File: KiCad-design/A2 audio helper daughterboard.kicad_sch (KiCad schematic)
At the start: 3 parts, among them J15 PIN HEADER 2x6, J16 SJ1-3515N

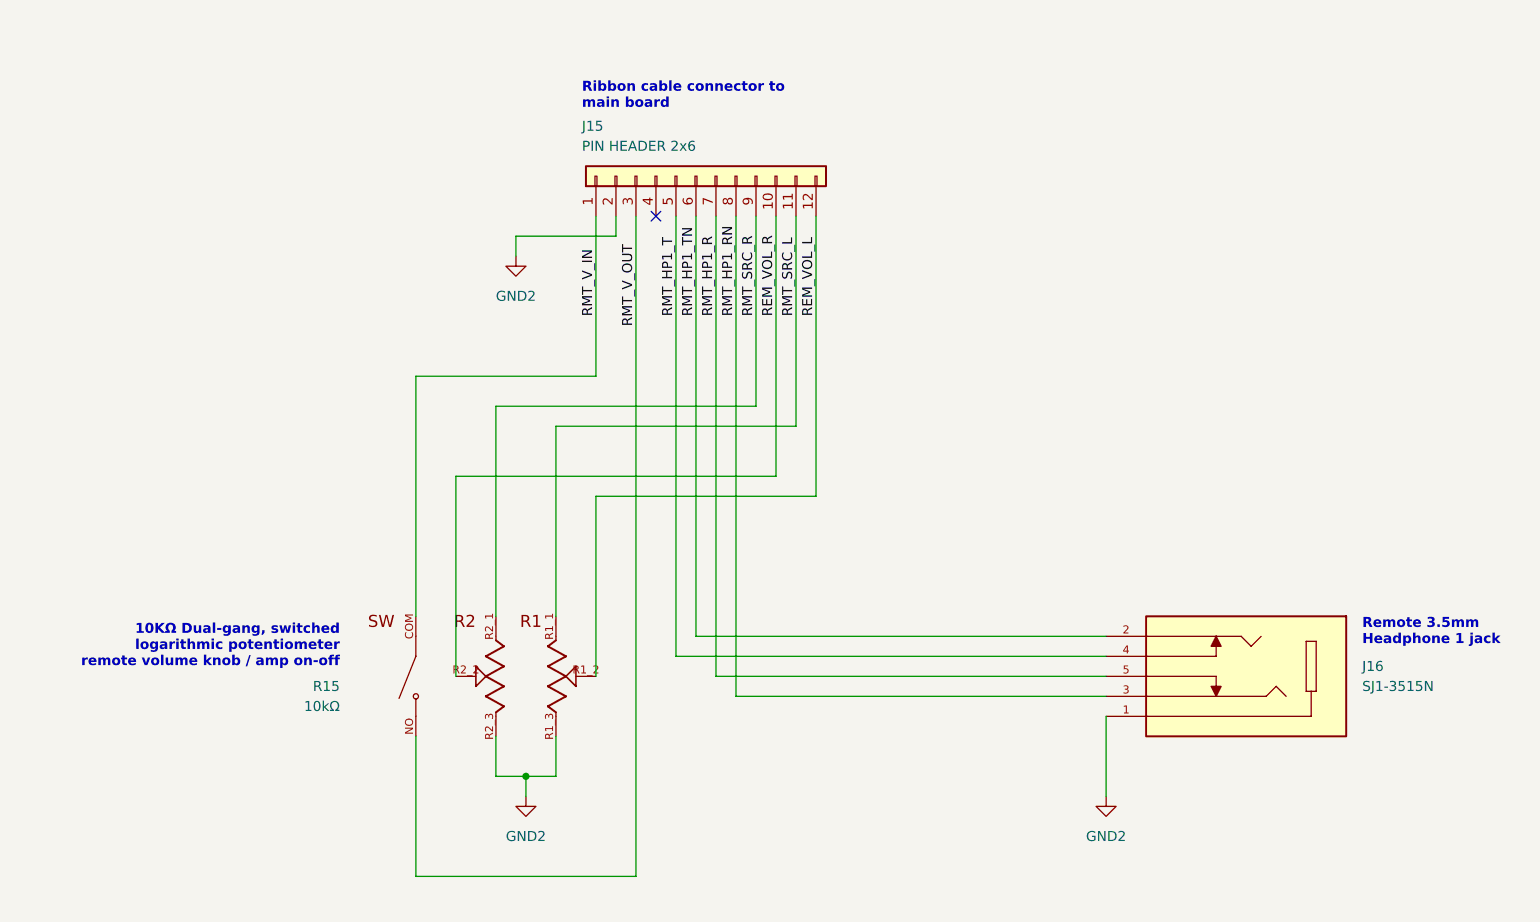
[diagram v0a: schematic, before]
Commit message: fixed dual headphones
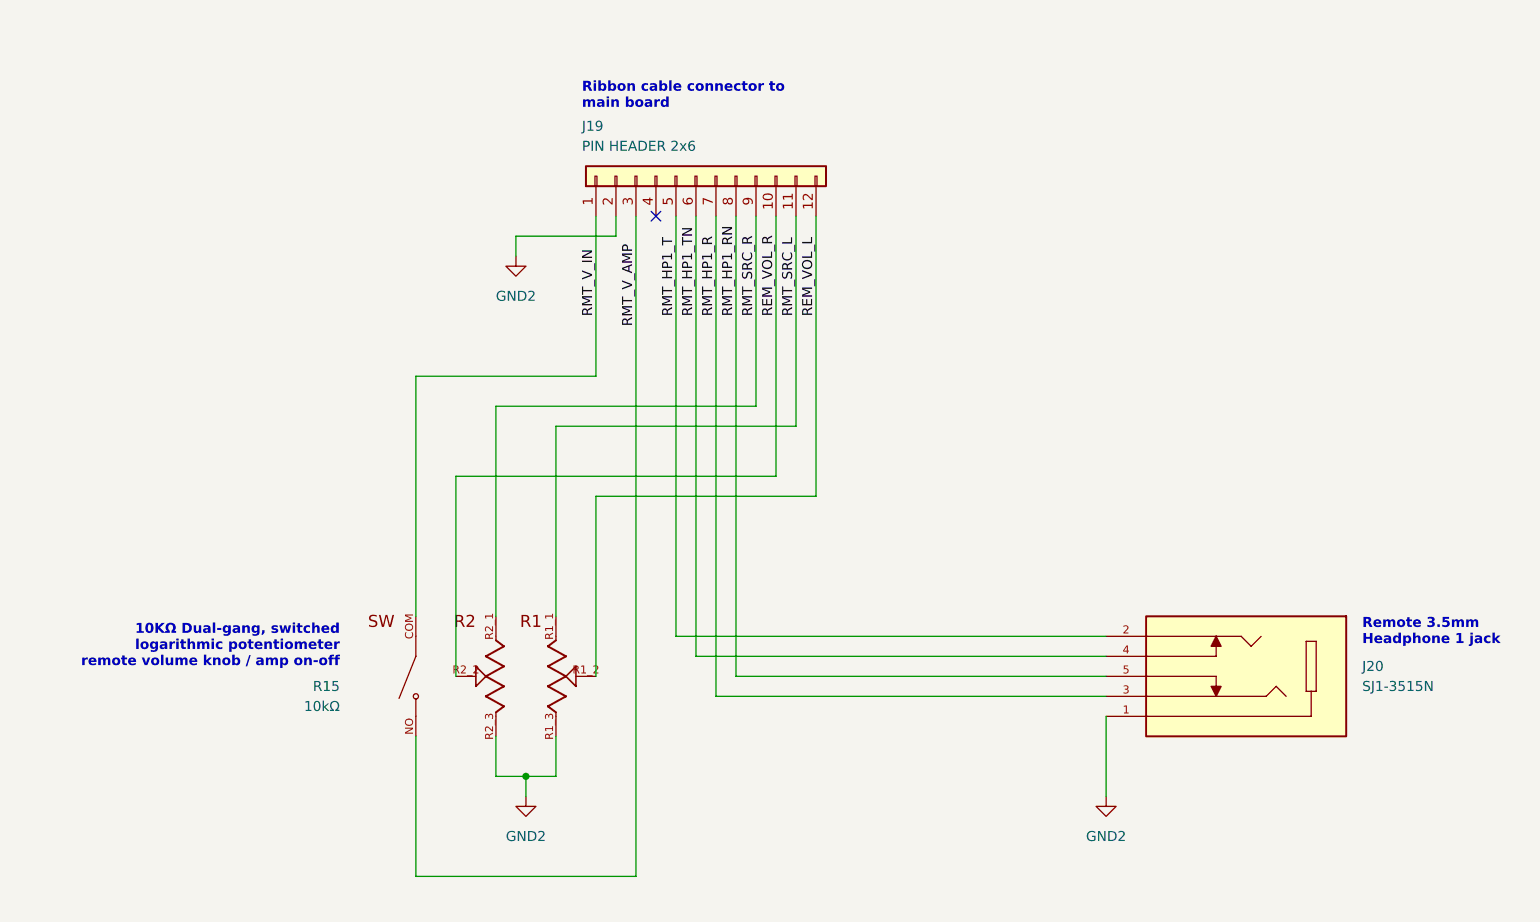
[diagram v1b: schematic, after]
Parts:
- renumbered J15 to J19, J16 to J20
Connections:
- net RMT_HP1_R: now also J20.3; no longer J20.5
- net RMT_HP1_RN: now also J20.5; no longer J20.3
- net RMT_HP1_T: now also J20.2; no longer J20.4
- net RMT_HP1_TN: now also J20.4; no longer J20.2
- net RMT_V_OUT renamed RMT_V_AMP
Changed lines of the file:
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@@
 	(title_block
 		(title "Apple 2 Audio Helper (daughterboard)")
-		(date "2026-01-24")
-		(rev "0.8")
+		(date "2026-01-28")
+		(rev "0.9")
 		(company "Northwest Retroventures")
 		(comment 2 "so those components can instead mount flush against angled base of Apple 2 case.")
 		(comment 3 "Use this instead of populating volume knob and headphone jack 1 on main board")
-		(comment 4 "Optional daughterboard connected via ribbon cable.")
+		(comment 4 "Circuit to mount in Apple 2 case beneath keyboard, exposing headph. jack & volume knob.")
 	)
 	(text "10KΩ Dual-gang, switched\nlogarithmic potentiometer\nremote volume knob / amp on-off"
@@
 	(wire
 		(pts
-			(xy 113.03 50.8) (xy 113.03 104.14)
+			(xy 113.03 50.8) (xy 113.03 106.68)
 		)
 		(stroke
@@
 	(wire
 		(pts
-			(xy 110.49 106.68) (xy 165.1 106.68)
-		)
-		(stroke
-			(width 0)
-			(type default)
-		)
-	)
-	(wire
-		(pts
-			(xy 115.57 50.8) (xy 115.57 109.22)
-		)
-		(stroke
-			(width 0)
-			(type default)
-		)
-	)
-	(wire
-		(pts
-			(xy 118.11 50.8) (xy 118.11 111.76)
+			(xy 110.49 104.14) (xy 165.1 104.14)
+		)
+		(stroke
+			(width 0)
+			(type default)
+		)
+	)
+	(wire
+		(pts
+			(xy 115.57 50.8) (xy 115.57 111.76)
+		)
+		(stroke
+			(width 0)
+			(type default)
+		)
+	)
+	(wire
+		(pts
+			(xy 118.11 50.8) (xy 118.11 109.22)
 		)
 		(stroke
@@
 	(wire
 		(pts
-			(xy 113.03 104.14) (xy 165.1 104.14)
+			(xy 113.03 106.68) (xy 165.1 106.68)
 		)
 		(stroke
@@
 	(wire
 		(pts
-			(xy 110.49 50.8) (xy 110.49 106.68)
+			(xy 110.49 50.8) (xy 110.49 104.14)
 		)
 		(stroke
@@
 	(wire
 		(pts
-			(xy 118.11 111.76) (xy 165.1 111.76)
+			(xy 118.11 109.22) (xy 165.1 109.22)
 		)
 		(stroke
@@
 	(wire
 		(pts
-			(xy 115.57 109.22) (xy 165.1 109.22)
+			(xy 115.57 111.76) (xy 165.1 111.76)
 		)
 		(stroke
@@
 		)
 	)
-	(label "RMT_V_OUT"
+	(label "RMT_V_AMP"
 		(at 105.41 64.77 90)
 		(effects
@@
 		(on_board yes)
 		(dnp no)
-		(property "Reference" "J16"
+		(property "Reference" "J20"
 			(at 197.612 107.95 0)
 			(effects
@@
 			(project "A2 audio helper 2"
 				(path "/5bdcff91-125f-4cf8-8ef8-6f244f2a71f5/03fd1e11-28b7-476a-9b76-001ec1c19924"
-					(reference "J16")
+					(reference "J20")
 					(unit 1)
 				)
@@
 		(on_board yes)
 		(dnp no)
-		(property "Reference" "J15"
+		(property "Reference" "J19"
 			(at 98.552 39.37 90)
 			(effects
@@
 			(project "A2 audio helper 2"
 				(path "/5bdcff91-125f-4cf8-8ef8-6f244f2a71f5/03fd1e11-28b7-476a-9b76-001ec1c19924"
-					(reference "J15")
+					(reference "J19")
 					(unit 1)
 				)

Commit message: made power & speaker input connectors also horizontal
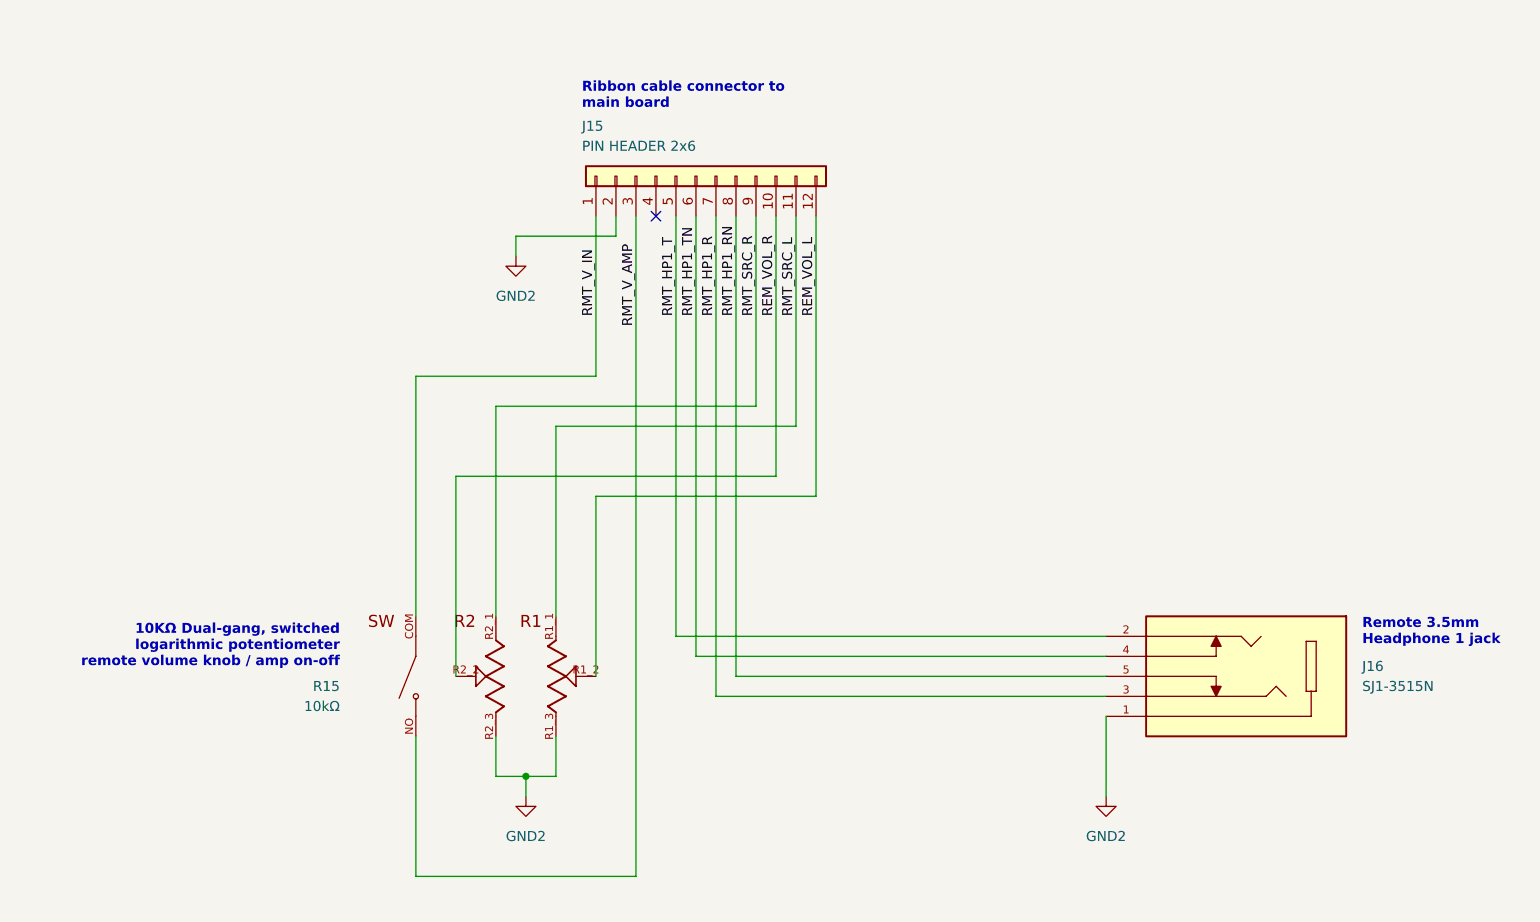
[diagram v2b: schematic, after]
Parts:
- renumbered J19 to J15, J20 to J16
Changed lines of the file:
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@@
 	(title_block
 		(title "Apple 2 Audio Helper (daughterboard)")
-		(date "2026-01-28")
-		(rev "0.9")
+		(date "2026-02-06")
+		(rev "0.10.1")
 		(company "Northwest Retroventures")
 		(comment 2 "so those components can instead mount flush against angled base of Apple 2 case.")
@@
 		(on_board yes)
 		(dnp no)
-		(property "Reference" "J20"
+		(property "Reference" "J16"
 			(at 197.612 107.95 0)
 			(effects
@@
 			(project "A2 audio helper 2"
 				(path "/5bdcff91-125f-4cf8-8ef8-6f244f2a71f5/03fd1e11-28b7-476a-9b76-001ec1c19924"
-					(reference "J20")
+					(reference "J16")
 					(unit 1)
 				)
@@
 		(on_board yes)
 		(dnp no)
-		(property "Reference" "J19"
+		(property "Reference" "J15"
 			(at 98.552 39.37 90)
 			(effects
@@
 			(project "A2 audio helper 2"
 				(path "/5bdcff91-125f-4cf8-8ef8-6f244f2a71f5/03fd1e11-28b7-476a-9b76-001ec1c19924"
-					(reference "J19")
+					(reference "J15")
 					(unit 1)
 				)

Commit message: added recommended decoupling cap to amp pwr/gnd
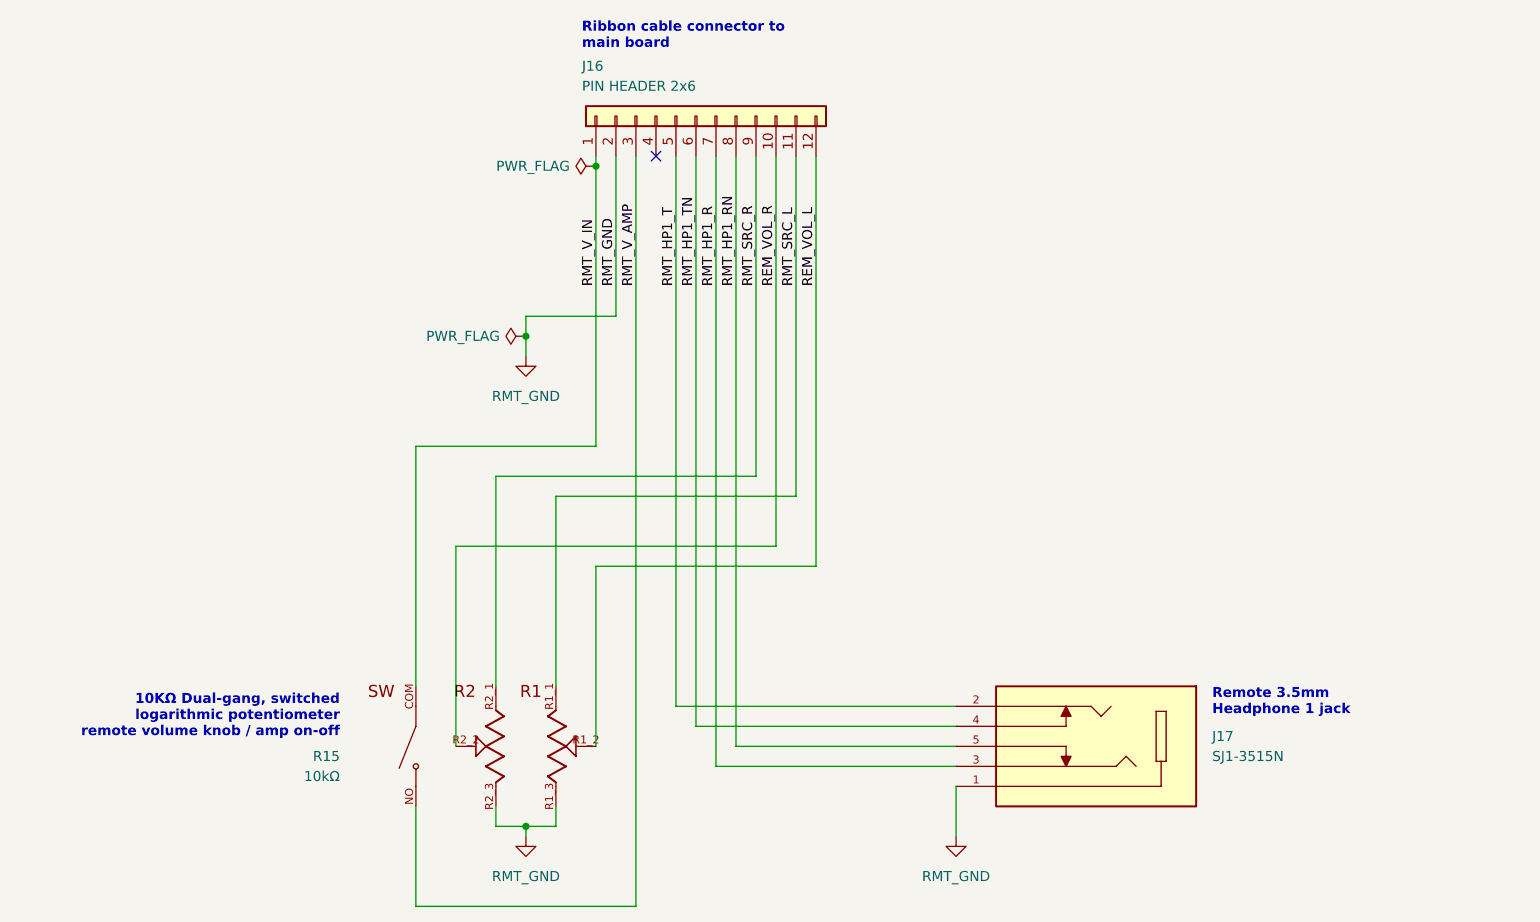
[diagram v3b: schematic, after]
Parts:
- renumbered J15 to J16, J16 to J17
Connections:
- net GND2 renamed RMT_GND
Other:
- moved on the sheet: J16, J17, R15

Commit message: change 3d model for vol knob
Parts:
- R15: footprint PTR902-1020K-A502:TRIM_PTR902-1020K-A502 -> PTN09S2_H10215K1A:TRIM_PTN09S2-H10215K1A
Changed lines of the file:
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@@
 	(title_block
 		(title "Apple 2 Audio Helper (daughterboard)")
-		(date "2026-02-18")
-		(rev "0.10.5")
+		(date "2026-02-26")
+		(rev "0.10.6")
 		(company "Northwest Retroventures")
 		(comment 2 "so those components can instead mount flush against angled base of Apple 2 case.")
@@
 			)
 		)
-		(property "Footprint" "PTR902-1020K-A502:TRIM_PTR902-1020K-A502"
+		(property "Footprint" "PTN09S2_H10215K1A:TRIM_PTN09S2-H10215K1A"
 			(at 87.63 118.11 0)
 			(effects

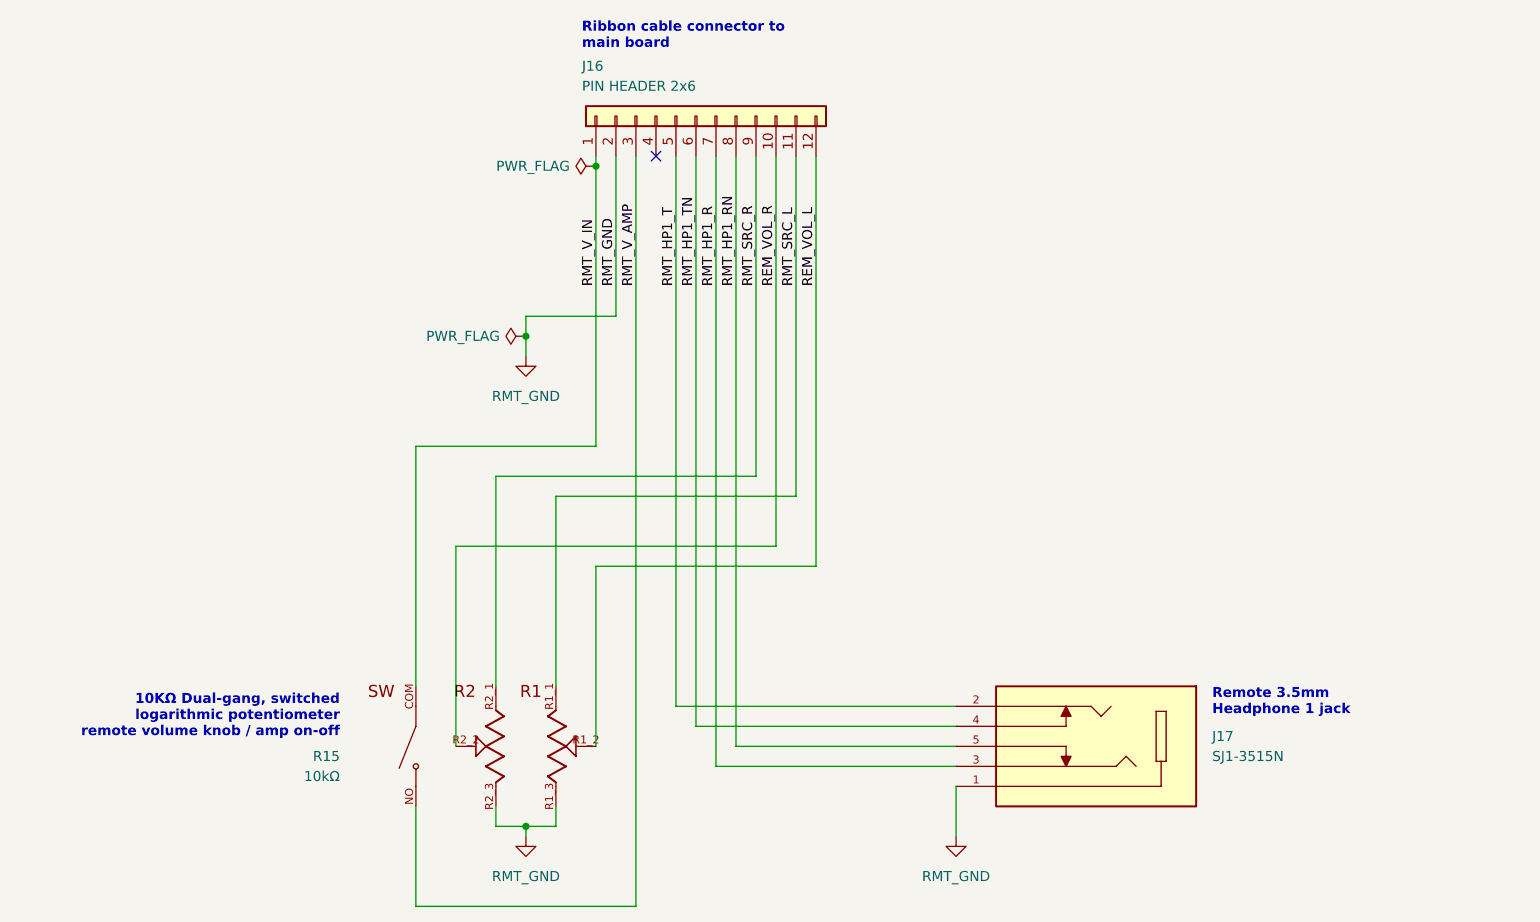
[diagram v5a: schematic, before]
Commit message: picked new part for front hp jack
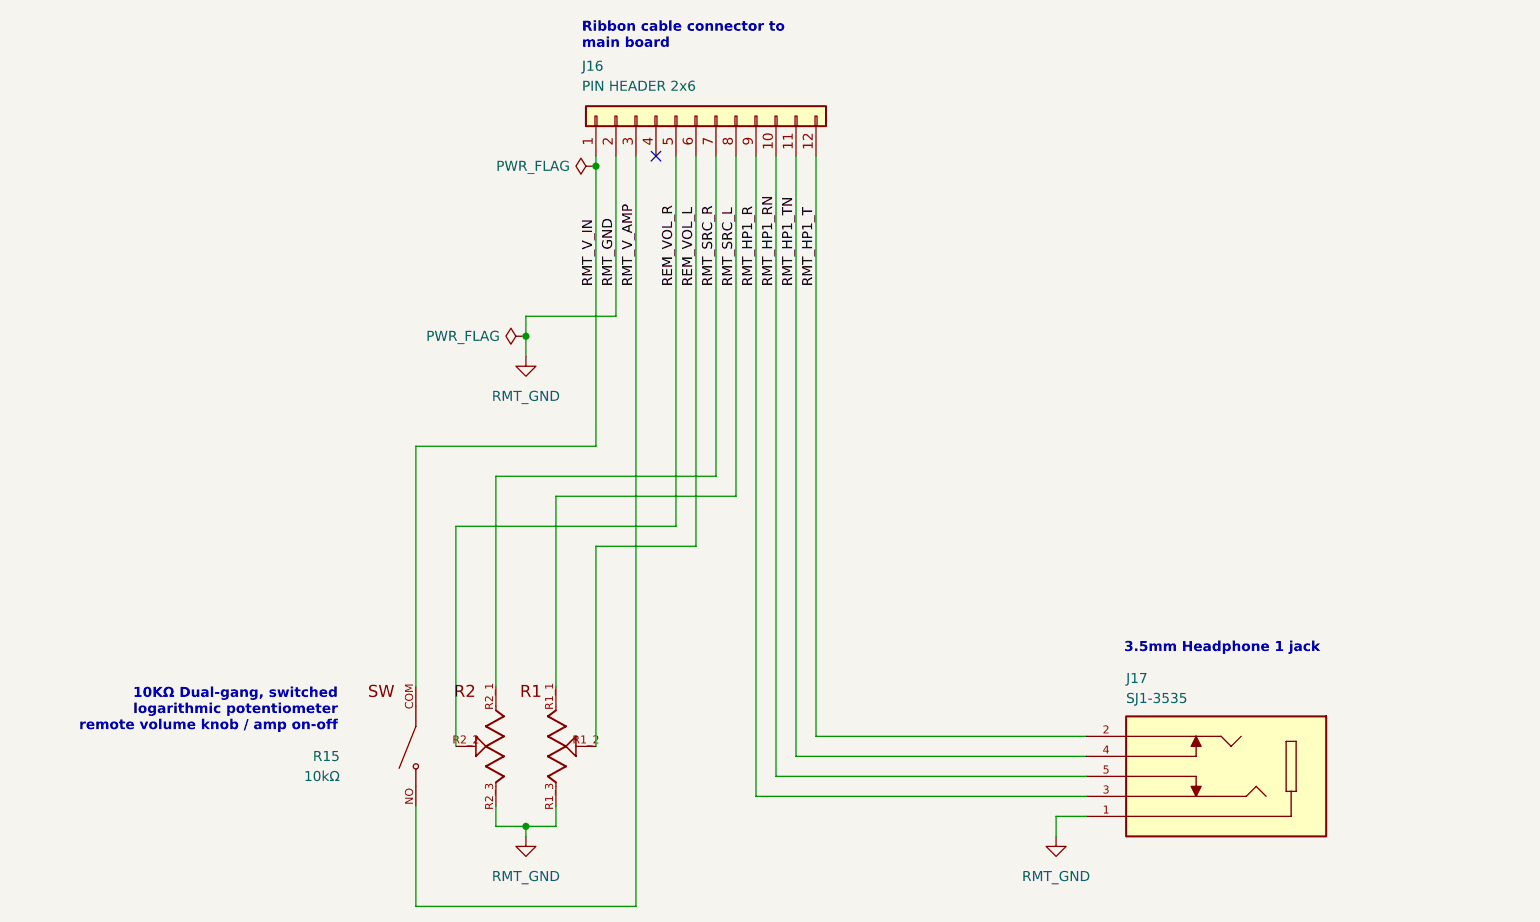
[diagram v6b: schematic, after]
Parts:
- J17: value SJ1-3515N -> SJ1-3535; footprint SJ1-3515N:CUI_SJ1-3515N -> SJ1-3535:CUI_SJ1-3535
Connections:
- net REM_VOL_L: now also J16.6 (Pin_6); no longer J16.12 (Pin_12)
- net REM_VOL_R: now also J16.5 (Pin_5); no longer J16.10 (Pin_10)
- net RMT_HP1_R: now also J16.9 (Pin_9); no longer J16.7 (Pin_7)
- net RMT_HP1_RN: now also J16.10 (Pin_10); no longer J16.8 (Pin_8)
- net RMT_HP1_T: now also J16.12 (Pin_12); no longer J16.5 (Pin_5)
- net RMT_HP1_TN: now also J16.11 (Pin_11); no longer J16.6 (Pin_6)
- net RMT_SRC_L: now also J16.8 (Pin_8); no longer J16.11 (Pin_11)
- net RMT_SRC_R: now also J16.7 (Pin_7); no longer J16.9 (Pin_9)
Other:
- note added: "3.5mm Headphone 1 jack"
- note removed: "Remote 3.5mm Headphone 1 jack"
